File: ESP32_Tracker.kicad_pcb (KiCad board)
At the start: 2 copper layers, 61 parts, among them J1 USB_C_Receptacle_USB2.0_16P, J2 Conn_01x02_Socket, J3 Micro_SD_Card_Det1, SW1 SW_Push, SW2 SW_Push, SW3 SW_Push, U1 XC6220B331MR-G, U2 USBLC6-2SC6, U3 MP2667, U4 SAM-M10Q, U5 LIS2MDL, U6 ESP32-S3-MINI-1

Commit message: initial board layout completed
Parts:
- added C19: 10u, Capacitor_SMD:C_0805_2012Metric, F.Cu at (134.3, 97.2)
- added C20: 0.1u, Capacitor_SMD:C_0805_2012Metric, F.Cu at (132.1, 97.2)
- added C21: 0.1u, Capacitor_SMD:C_0805_2012Metric, B.Cu at (143.8, 105.2)
- added C22: 10u, Capacitor_SMD:C_0805_2012Metric, B.Cu at (141.6, 105.2)
- added J4: MSD-4-A, MSD-4-A_DL:CUI_MSD-4-A, B.Cu at (154.8, 105.5)
- added R19: 10k, Resistor_SMD:R_0805_2012Metric, B.Cu at (142.6, 108.7)
- added R20: 10k, Resistor_SMD:R_0805_2012Metric, B.Cu at (143.7, 99.7)
- added R21: 10k, Resistor_SMD:R_0805_2012Metric, F.Cu at (132.8, 106.0)
- added R22: 10k, Resistor_SMD:R_0805_2012Metric, B.Cu at (142.6, 111.0)
- added R23: 10k, Resistor_SMD:R_0805_2012Metric, B.Cu at (143.7, 97.7)
- added SW4: SW_Push, Button_Switch_SMD:SW_SPST_TS-1088-xR020, F.Cu at (152.6, 103.2)
- added SW5: SW_Push, Button_Switch_SMD:SW_SPST_TL3305C, F.Cu at (158.1, 93.0)
- C1, C5: value 10u -> 1u
- C10: value 0.1u -> 2.2u
- C11, C13: value 0.1u -> 10u
- C12: value 22u -> 10u
- C15, C4: value 10u -> 0.1u
- C16: value 1u -> 0.22u
- C17: value 0.22u -> 2.2u
- C2: value 1u -> 0.1u
- C3: value 2.2u -> 22u
- C7: value 2.2u -> 0.1u
- J3: value Micro_SD_Card_Det1 -> Conn_01x07_Socket; footprint MSD-4-A_DL:CUI_MSD-4-A -> Connector_JST:JST_XH_S7B-XH-A_1x07_P2.50mm_Horizontal
- R1, R3: value 5.1k -> 10k
- R13: value 10k -> 100k
- R16, R2: value 10k -> 2.2k
- R18, TP1, TP2, TP3, TP4, TP5, TP6, TP7, TP8: moved to B.Cu
- R5: value 100k -> 5.1k
- R6: value 2.2k -> 5.1k
- R7: value 2.2k -> 10k
- U1: value XC6220B331MR-G -> USBLC6-2SC6; footprint Package_TO_SOT_SMD:SOT-23-5 -> Package_TO_SOT_SMD:SOT-23-6
- U2: value USBLC6-2SC6 -> ESP32-S3-MINI-1; footprint Package_TO_SOT_SMD:SOT-23-6 -> RF_Module:ESP32-S2-MINI-1
- U4: value SAM-M10Q -> XC6220B331MR-G; footprint RF_GPS:ublox_SAM-M8Q -> Package_TO_SOT_SMD:SOT-23-5
- U6: value ESP32-S3-MINI-1 -> SAM-M10Q; footprint RF_Module:ESP32-S2-MINI-1 -> RF_GPS:ublox_SAM-M8Q
- moved TP8 81.7 mm to (125.6, 68.2)
- moved SW1 76.1 mm to (121.1, 117.5)
- moved TP5 73.6 mm to (124.3, 74.0)
- moved H3 72.4 mm to (121.3, 132.2)
- moved TP2 66.5 mm to (122.3, 82.5)
- moved TP3 65.0 mm to (122.3, 85.7)
- moved TP4 59.5 mm to (128.8, 89.7)
- moved TP1 58.7 mm to (152.3, 68.0)
- moved SW3 57.0 mm to (124.3, 74.0), turned to 90 degrees
- moved J1 57.0 mm to (121.8, 85.0), turned to -90 degrees
- moved U1 56.3 mm to (130.3, 85.0)
- moved R6 55.1 mm to (123.6, 78.5)
- moved H2 54.2 mm to (121.1, 68.2)
- moved U2 53.7 mm to (140.3, 70.7)
- moved U5 52.8 mm to (155.1, 76.0)
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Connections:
- C1 pad 1: +3.3V -> Net-(U2-EN)
- C10 pad 1: +3.3V -> Net-(U3-SYS)
- C11 pad 1: +3.3V -> GND
- C11 pad 2: GND -> Net-(U3-SYS)
- C16 pad 1: Net-(U6-EN) -> Net-(U5-C1)
- C17 pad 1: Net-(U5-C1) -> +3.3V
- C18 pad 1: Net-(U6-IO21) -> +3.3V
- C2 pad 1: GND -> Net-(U2-IO18)
- C2 pad 2: VBUS -> GND
- C3 pad 1: Net-(U1-CE) -> +3.3V
- C4 pad 1: GND -> +3.3V
- C4 pad 2: Net-(U1-CE) -> GND
- C5 pad 2: Net-(J2-Pin_2) -> VBUS
- C6 pad 1: Net-(U3-VDD) -> Net-(U2-IO42)
- C7 pad 1: +3.3V -> Net-(U2-IO21)
- C8 pad 1: +3.3V -> Net-(U3-VDD)
- C9 pad 1: +3.3V -> GND
- C9 pad 2: GND -> Net-(J2-Pin_2)
- J3 pad 1: unconnected-(J3-DAT2-Pad1) -> GND
- J3 pad 2: /SD_CS -> +3.3V
- J3 pad 3: /SD_MOSI -> /MCU/PWR/OLED/SD_SCK
- J3 pad 4: +3.3V -> /MCU/PWR/OLED/SD_MOSI
- J3 pad 5: /SD_CLK -> /MCU/PWR/OLED_CS
- J3 pad 6: GND -> /MCU/PWR/OLED_DC
- J3 pad 7: /SD_MISO -> /MCU/PWR/OLED_RST
- R1 pad 1: GND -> Net-(U2-EN)
- R1 pad 2: Net-(J1-CC1) -> +3.3V
- R10 pad 1: /MAG_DATA -> Net-(U3-NTC)
- R10 pad 2: +3.3V -> VBUS
- R11 pad 1: /MAG_CLK -> Net-(U2-IO42)
- R12 pad 1: /SD_CS -> Net-(U2-IO21)
- R13 pad 1: /SD_MOSI -> +3.3V
- R13 pad 2: +3.3V -> /MCU/PWR/INT
- R14 pad 1: /SD_CLK -> /MCU/PWR/GPS/MAG_DATA
- R15 pad 1: /SD_MISO -> /MCU/PWR/GPS/MAG_CLK
- R16 pad 1: /SD_DETECT -> /MCU/PWR/GPS/MAG_CLK
- R17 pad 1: Net-(D1-A) -> /MCU/PWR/GPS/MAG_DATA
- R17 pad 2: Net-(U6-IO42) -> +3.3V
- R18 pad 1: Net-(U6-IO21) -> +3.3V
- R18 pad 2: +3.3V -> /MCU/PWR/OLED/SD_SCK
- R2 pad 1: Net-(U3-NTC) -> Net-(U2-IO8)
- R2 pad 2: VBUS -> Net-(D1-A)
- R3 pad 1: Net-(J1-CC2) -> Net-(U2-IO18)
- R3 pad 2: GND -> +3.3V
- R4 pad 1: Net-(U3-NTC) -> Net-(U2-IO0)
- R4 pad 2: GND -> +3.3V
- R5 pad 1: +3.3V -> GND
- R5 pad 2: /INT -> Net-(J1-CC1)
- R6 pad 1: /GPS_CLK -> Net-(J1-CC2)
- R6 pad 2: +3.3V -> GND
- R7 pad 1: /GPS_DATA -> /MCU/PWR/BATT_CLK
- R8 pad 1: Net-(U6-EN) -> +3.3V
- R8 pad 2: +3.3V -> /MCU/PWR/BATT_DATA
- R9 pad 1: Net-(U6-IO0) -> Net-(U3-NTC)
- R9 pad 2: +3.3V -> GND
- SW1 pad 2: Net-(U6-EN) -> Net-(U2-EN)
- SW2 pad 1: Net-(U6-IO0) -> Net-(U2-IO18)
- SW3 pad 1: Net-(U6-IO21) -> Net-(U2-IO0)
- TP1 pad 1: VBUS -> Net-(U2-EN)
- TP2 pad 1: +3.3V -> Net-(J1-D--PadA7)
- TP3 pad 1: Net-(U6-EN) -> Net-(J1-D+-PadA6)
- TP4 pad 1: Net-(U6-IO0) -> VBUS
- TP5 pad 1: Net-(J1-D--PadA7) -> Net-(U2-IO0)
- TP6 pad 1: Net-(J1-D+-PadA6) -> Net-(J2-Pin_2)
- TP7 pad 1: Net-(J2-Pin_2) -> Net-(U3-SYS)
- TP8 pad 1: Net-(U1-CE) -> +3.3V
- U1 pad 1: Net-(U1-CE) -> Net-(J1-D--PadA7)
- U1 pad 3: Net-(U1-CE) -> Net-(J1-D+-PadA6)
- U1 pad 4: unconnected-(U1-NC-Pad4) -> /MCU/PWR/USB_P
- U1 pad 5: +3.3V -> VBUS
- U2 pad 1: Net-(J1-D--PadA7) -> GND
- U2 pad 3: Net-(J1-D+-PadA6) -> +3.3V
- U2 pad 4: /USB_P -> Net-(U2-IO0)
- U2 pad 5: VBUS -> unconnected-(U2-IO1-Pad5)
- U2 pad 6: /USB_N -> unconnected-(U2-IO2-Pad6)
- U3 pad 10: Net-(U1-CE) -> Net-(U3-SYS)
- U3 pad 3: /INT -> /MCU/PWR/INT
- U3 pad 6: /BATT_CLK -> /MCU/PWR/BATT_CLK
- U3 pad 7: /BATT_DATA -> /MCU/PWR/BATT_DATA
- U4 pad 1: GND -> Net-(U3-SYS)
- U4 pad 2: +3.3V -> GND
- U4 pad 3: +3.3V -> Net-(U3-SYS)
- U4 pad 4: GND -> unconnected-(U4-NC-Pad4)
- U4 pad 5: GND -> +3.3V
- U5 pad 1: /MAG_CLK -> /MCU/PWR/GPS/MAG_CLK
- U5 pad 4: /MAG_DATA -> /MCU/PWR/GPS/MAG_DATA
- U5 pad 7: /MAG_INT -> /MCU/PWR/MAG_INT
- U6 pad 10: /GPS_CLK -> GND
- U6 pad 11: unconnected-(U6-IO7-Pad11) -> GND
- U6 pad 12: unconnected-(U6-IO8-Pad12) -> /MCU/PWR/GPS/MAG_CLK
- U6 pad 13: /SD_DETECT -> unconnected-(U6-TXD-Pad13)
- U6 pad 14: /SD_CS -> unconnected-(U6-RXD-Pad14)
- U6 pad 15: /SD_MOSI -> GND
- U6 pad 16: /SD_CLK -> GND
- U6 pad 17: /SD_MISO -> +3.3V
- U6 pad 18: /MAG_DATA -> unconnected-(U6-~{RESET}-Pad18)
- U6 pad 19: /MAG_CLK -> unconnected-(U6-EXTINT-Pad19)
- U6 pad 2: GND -> +3.3V
- U6 pad 20: /MAG_INT -> GND
- U6 pad 4: Net-(U6-IO0) -> GND
- U6 pad 5: unconnected-(U6-IO1-Pad5) -> GND
- U6 pad 6: unconnected-(U6-IO2-Pad6) -> GND
- U6 pad 9: /GPS_DATA -> /MCU/PWR/GPS/MAG_DATA
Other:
- board outline added: 45.5 x 75.5 mm
- copper layers 2 -> 4

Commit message: Layout completed
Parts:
- removed H4: MountingHole_Pad, MountingHole:MountingHole_2.2mm_M2_Pad_Via
- added J5: Conn_01x07_Socket, Connector_JST:JST_PH_S7B-PH-K_1x07_P2.00mm_Horizontal, F.Cu at (167.2, 116.0)
- C17: value 2.2u -> 10u; moved to B.Cu
- C18, R16, R17: moved to B.Cu
- C21, C22, J4, R18, R19, R20, R22, R23: moved to F.Cu
- J3: value Conn_01x07_Socket -> Conn_01x03; footprint Connector_JST:JST_XH_S7B-XH-A_1x07_P2.50mm_Horizontal -> Connector_PinHeader_2.54mm:PinHeader_1x03_P2.54mm_Vertical
- SW2, SW4: footprint Button_Switch_SMD:SW_SPST_TS-1088-xR020 -> Button_Switch_SMD:SW_SPST_TL3305C
- moved H2 81.2 mm to (170.1, 133.0)
- moved D1 63.0 mm to (127.2, 70.8), turned to 90 degrees
- moved SW1 61.8 mm to (170.2, 80.0), turned to 180 degrees
- moved R2 60.2 mm to (129.3, 70.8), turned to 90 degrees
- moved C1 57.0 mm to (165.9, 79.5), turned to 90 degrees
- moved R1 53.0 mm to (163.7, 79.4)
- moved SW3 45.8 mm to (170.2, 75.8), turned to 0 degrees
- moved C14 44.9 mm to (127.8, 104.5)
- moved C13 43.5 mm to (130.1, 108.3)
- moved C15 41.5 mm to (130.1, 104.5)
- moved J2 40.5 mm to (120.8, 68.0), turned to 180 degrees
- moved J3 39.4 mm to (160.5, 74.5), turned to 180 degrees
- moved R4 38.8 mm to (166.2, 74.7)
- moved TP6 38.3 mm to (123.0, 75.5)
- moved C20 36.6 mm to (164.2, 115.0), turned to -90 degrees
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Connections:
- net Net-(J2-Pin_2) renamed +BATT
- C2 pad 1: Net-(U2-IO18) -> /MCU/PWR/SW_TOGGLE
- C6 pad 1: Net-(U2-IO42) -> /MCU/PWR/SW_PWR
- C7 pad 1: Net-(U2-IO21) -> /MCU/PWR/SW_LOG
- J1 pad A6: Net-(J1-D+-PadA6) -> unconnected-(J1-D+-PadA6)
- J1 pad A7: Net-(J1-D--PadA7) -> unconnected-(J1-D--PadA7)
- J1 pad B6: Net-(J1-D+-PadA6) -> unconnected-(J1-D+-PadB6)
- J1 pad B7: Net-(J1-D--PadA7) -> unconnected-(J1-D--PadB7)
- J3 pad 1: GND -> /MCU/PWR/TX
- J3 pad 2: +3.3V -> /MCU/PWR/RX
- J3 pad 3: /MCU/PWR/OLED/SD_SCK -> GND
- R11 pad 1: Net-(U2-IO42) -> /MCU/PWR/SW_PWR
- R12 pad 1: Net-(U2-IO21) -> /MCU/PWR/SW_LOG
- R13 pad 2: /MCU/PWR/INT -> /MCU/PWR/BATT_INT
- R2 pad 1: Net-(U2-IO8) -> Net-(U2-IO2)
- R3 pad 1: Net-(U2-IO18) -> /MCU/PWR/SW_TOGGLE
- SW2 pad 1: Net-(U2-IO18) -> GND
- SW2 pad 2: GND -> /MCU/PWR/SW_TOGGLE
- SW4 pad 1: Net-(U2-IO42) -> /MCU/PWR/SW_PWR
- SW5 pad 1: Net-(U2-IO21) -> /MCU/PWR/SW_LOG
- TP2 pad 1: Net-(J1-D--PadA7) -> /MCU/PWR/TX
- TP3 pad 1: Net-(J1-D+-PadA6) -> /MCU/PWR/RX
- U1 pad 1: Net-(J1-D--PadA7) -> unconnected-(U1-I/O1-Pad1)
- U1 pad 3: Net-(J1-D+-PadA6) -> unconnected-(U1-I/O2-Pad3)
- U1 pad 4: /MCU/PWR/USB_P -> unconnected-(U1-I/O2-Pad4)
- U1 pad 6: /MCU/PWR/USB_N -> unconnected-(U1-I/O1-Pad6)
- U2 pad 10: /MCU/PWR/GPS/MAG_CLK -> /MCU/PWR/BATT_INT
- U2 pad 11: /MCU/PWR/OLED_CS -> unconnected-(U2-IO7-Pad11)
- U2 pad 12: Net-(U2-IO8) -> unconnected-(U2-IO8-Pad12)
- U2 pad 13: /MCU/PWR/SD_DETECT -> unconnected-(U2-IO9-Pad13)
- U2 pad 14: /MCU/PWR/SD_CS -> unconnected-(U2-IO10-Pad14)
- U2 pad 15: /MCU/PWR/OLED/SD_MOSI -> unconnected-(U2-IO11-Pad15)
- U2 pad 16: /MCU/PWR/OLED/SD_SCK -> /MCU/PWR/MAG_INT
- U2 pad 17: /MCU/PWR/SD_MISO -> /MCU/PWR/GPS/MAG_DATA
- U2 pad 18: unconnected-(U2-IO14-Pad18) -> /MCU/PWR/GPS/MAG_CLK
- U2 pad 19: unconnected-(U2-IO15-Pad19) -> /MCU/PWR/SD_DETECT
- U2 pad 20: /MCU/PWR/MAG_INT -> /MCU/PWR/SD_MISO
- U2 pad 21: unconnected-(U2-IO17-Pad21) -> /MCU/PWR/OLED/SD_SCK
- U2 pad 22: Net-(U2-IO18) -> /MCU/PWR/OLED/SD_MOSI
- U2 pad 23: /MCU/PWR/USB_N -> unconnected-(U2-USB_D--Pad23)
- U2 pad 24: /MCU/PWR/USB_P -> unconnected-(U2-USB_D+-Pad24)
- U2 pad 25: Net-(U2-IO21) -> /MCU/PWR/SD_CS
- U2 pad 26: /MCU/PWR/OLED_RST -> /MCU/PWR/OLED_CS
- U2 pad 28: unconnected-(U2-IO33-Pad28) -> /MCU/PWR/OLED_DC
- U2 pad 29: /MCU/PWR/BATT_DATA -> /MCU/PWR/OLED_RST
- U2 pad 31: /MCU/PWR/BATT_CLK -> unconnected-(U2-IO35-Pad31)
- U2 pad 33: unconnected-(U2-IO37-Pad33) -> /MCU/PWR/SW_LOG
- U2 pad 34: unconnected-(U2-IO38-Pad34) -> /MCU/PWR/SW_PWR
- U2 pad 35: unconnected-(U2-IO39-Pad35) -> /MCU/PWR/SW_TOGGLE
- U2 pad 38: Net-(U2-IO42) -> unconnected-(U2-IO42-Pad38)
- U2 pad 39: unconnected-(U2-TXD0-Pad39) -> /MCU/PWR/TX
- U2 pad 40: unconnected-(U2-RXD0-Pad40) -> /MCU/PWR/RX
- U2 pad 6: unconnected-(U2-IO2-Pad6) -> Net-(U2-IO2)
- U2 pad 8: /MCU/PWR/OLED_DC -> /MCU/PWR/BATT_DATA
- U2 pad 9: /MCU/PWR/GPS/MAG_DATA -> /MCU/PWR/BATT_CLK
- U3 pad 3: /MCU/PWR/INT -> /MCU/PWR/BATT_INT
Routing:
- net GND: track 0.00 -> 95.8 mm, vias 0 -> 183
- net +3.3V: track 0.00 -> 71.5 mm, vias 0 -> 29
- net /MCU/PWR/OLED/SD_SCK: track 0.00 -> 56.2 mm, vias 0 -> 2
- net /MCU/PWR/GPS/MAG_DATA: track 0.00 -> 54.7 mm, vias 0 -> 2
- net /MCU/PWR/OLED/SD_MOSI: track 0.00 -> 52.7 mm, vias 0 -> 2
- net /MCU/PWR/GPS/MAG_CLK: track 0.00 -> 50.0 mm, vias 0 -> 2
- net /MCU/PWR/SD_CS: track 0.00 -> 40.5 mm
- net /MCU/PWR/OLED_CS: track 0.00 -> 35.8 mm
- net /MCU/PWR/SD_MISO: track 0.00 -> 34.9 mm
- net /MCU/PWR/SD_DETECT: track 0.00 -> 34.6 mm
- net Net-(U2-IO0): track 0.00 -> 34.2 mm, vias 0 -> 2
- net /MCU/PWR/SW_LOG: track 0.00 -> 32.9 mm
- net /MCU/PWR/OLED_DC: track 0.00 -> 32.4 mm
- net /MCU/PWR/OLED_RST: track 0.00 -> 30.5 mm
- net /MCU/PWR/MAG_INT: track 0.00 -> 27.3 mm
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- added copper zone on F.Cu, net +3.3V
- added copper zone on In2.Cu, net +3.3V
- added copper zone on F.Cu, net +BATT
- added copper zone on B.Cu, net GND
- added copper zone on F.Cu, net GND
- added copper zone on In1.Cu, net GND
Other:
- board size 45.5 x 75.5 mm -> 60 x 75 mm
- board text added: "Matthew Tubbin REV 1.0 1/13/2026 ECE212"

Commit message: modified layout
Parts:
- added TP9: TestPoint, TestPoint:TestPoint_Pad_D1.5mm, B.Cu at (147.7, 88.5)
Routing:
- net +3.3V: track 71.5 -> 64.4 mm, vias 29 -> 34
- net GND: track 95.8 -> 99.2 mm, vias 183 -> 186
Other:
- board text added: "3.3V"
- board text added: "BATT"
- board text added: "BOOT"
- board text added: "GND"
- board text added: "LOG"
- board text added: "PWR"
- board text added: "RESET"
- board text added: "RX"
- board text added: "SYS"
- board text added: "TOGGLE"
- board text added: "TX"
- board text added: "VBUS"

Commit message: modified and labeled layout
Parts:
- added C23: 0.1u, Capacitor_SMD:C_0805_2012Metric, B.Cu at (116.8, 120.5)
- moved C17 5.74 mm to (127.3, 135.0), turned to 0 degrees
- moved C13 4.78 mm to (132.7, 104.3)
- moved C15 4.78 mm to (132.7, 100.5)
- moved C16 4.78 mm to (135.2, 96.8)
- moved R14 4.78 mm to (138.2, 95.5)
- moved U5 4.78 mm to (135.9, 100.2)
- moved C14 4.78 mm to (130.4, 100.5)
- moved R15 4.78 mm to (139.2, 100.2)
- moved TP5 3.76 mm to (144.2, 74.5)
- moved TP1 3.50 mm to (157.0, 72.8)
- moved C18 2.87 mm to (127.3, 132.8)
- moved R16 2.47 mm to (127.3, 113.7)
- moved U6 2.47 mm to (126.3, 123.5)
- moved R17 2.47 mm to (136.2, 122.4)
- moved R23 0.29 mm to (142.8, 112.8)
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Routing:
- net GND: track 99.2 -> 123.0 mm, vias 186 -> 218
- net /MCU/PWR/MAG_INT: track 27.3 -> 22.2 mm
- net +3.3V: track 64.4 -> 59.6 mm, vias 34 -> 33
- net Net-(U2-IO0): track 34.2 -> 31.3 mm
- net Net-(U2-EN): track 24.5 -> 22.1 mm
- net /MCU/PWR/GPS/MAG_CLK: track 50.0 -> 47.6 mm
- net /MCU/PWR/GPS/MAG_DATA: track 54.7 -> 52.3 mm
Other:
- board text added: "Matthew Tubbin REV 1.0 1/14/2026 ECE-212"
- board text removed: "Matthew Tubbin REV 1.0 1/13/2026 ECE212"

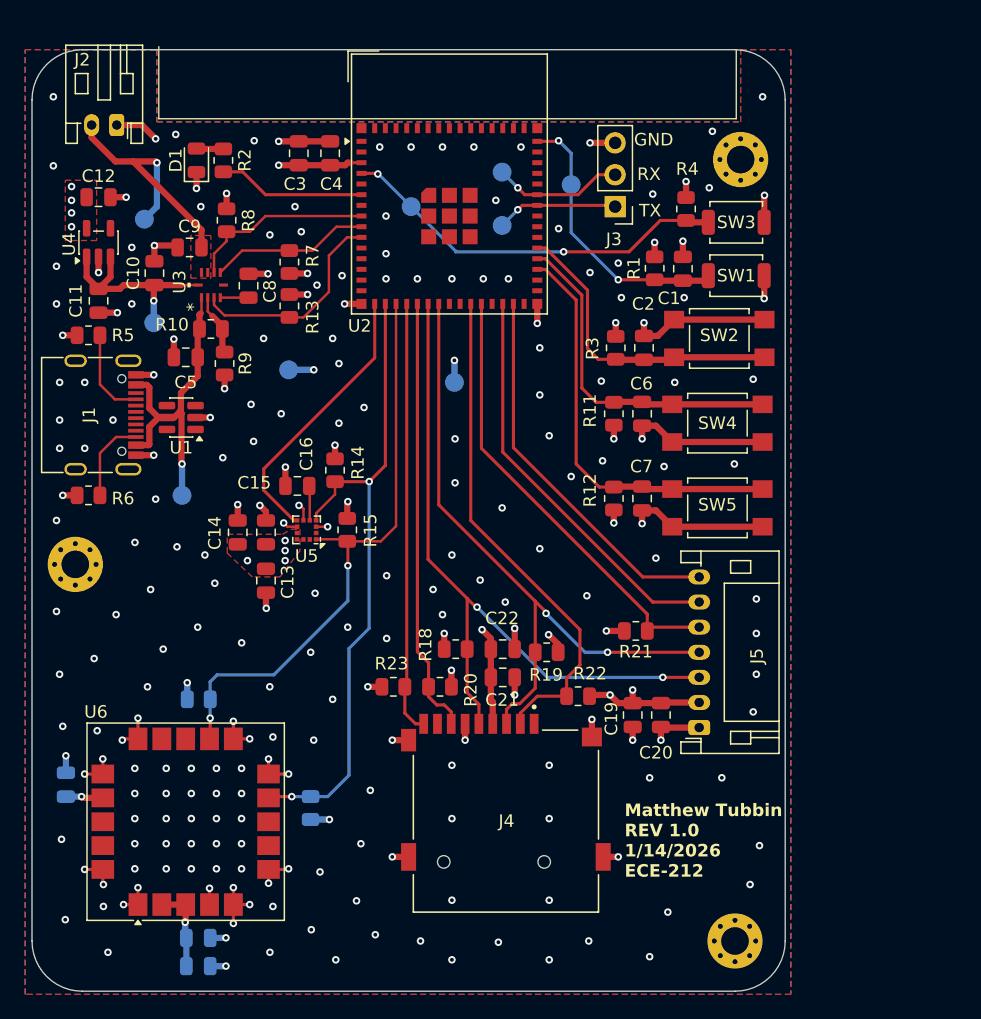
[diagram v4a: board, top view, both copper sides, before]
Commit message: added USBC programming
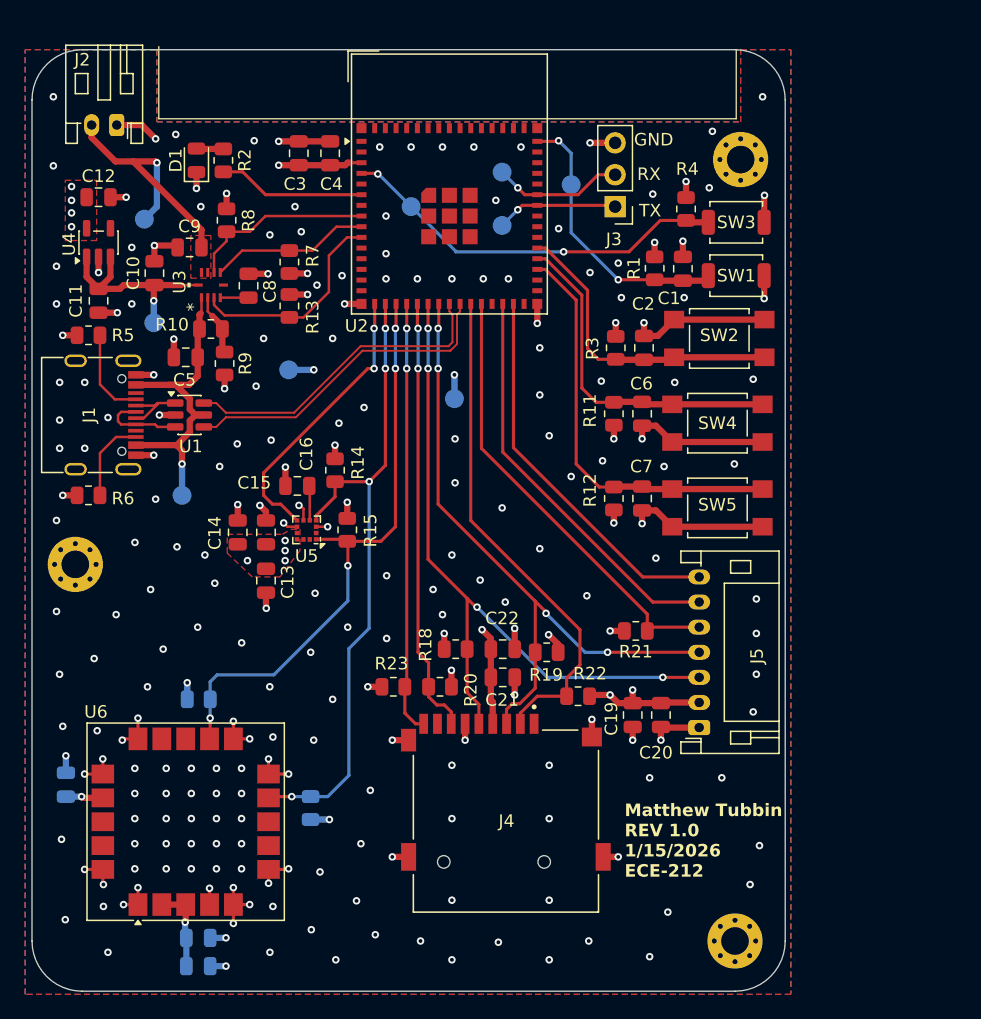
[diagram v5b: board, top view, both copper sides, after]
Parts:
- moved TP9 1.30 mm to (147.7, 89.8)
- moved U1 0.69 mm to (126.6, 91.1), turned to 0 degrees
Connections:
- J1 pad A6: unconnected-(J1-D+-PadA6) -> Net-(J1-D+-PadA6)
- J1 pad A7: unconnected-(J1-D--PadA7) -> Net-(J1-D--PadA7)
- J1 pad B6: unconnected-(J1-D+-PadB6) -> Net-(J1-D+-PadA6)
- J1 pad B7: unconnected-(J1-D--PadB7) -> Net-(J1-D--PadA7)
- U1 pad 1: unconnected-(U1-I/O1-Pad1) -> Net-(J1-D--PadA7)
- U1 pad 3: unconnected-(U1-I/O2-Pad3) -> Net-(J1-D+-PadA6)
- U1 pad 4: unconnected-(U1-I/O2-Pad4) -> /MCU/PWR/USB_D+
- U1 pad 6: unconnected-(U1-I/O1-Pad6) -> /MCU/PWR/USB_D-
- U2 pad 23: unconnected-(U2-USB_D--Pad23) -> /MCU/PWR/USB_D-
- U2 pad 24: unconnected-(U2-USB_D+-Pad24) -> /MCU/PWR/USB_D+
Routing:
- net /MCU/PWR/USB_D+: track 0.00 -> 26.2 mm
- net /MCU/PWR/USB_D-: track 0.00 -> 25.6 mm
- net Net-(J1-D+-PadA6): track 0.00 -> 6.77 mm
- net Net-(J1-D--PadA7): track 0.00 -> 5.50 mm
- net VBUS: track 25.8 -> 26.4 mm
- net /MCU/PWR/MAG_INT: track 22.2 -> 22.7 mm, vias 0 -> 2
- net GND: track 123.0 -> 123.2 mm, vias 218 -> 217
- net /MCU/PWR/OLED/SD_MOSI: track 52.7 -> 52.9 mm, vias 2 -> 4
- net /MCU/PWR/GPS/MAG_CLK: track 47.6 -> 47.7 mm, vias 2 -> 4
- net /MCU/PWR/SD_MISO: vias 0 -> 2
- net /MCU/PWR/SD_DETECT: vias 0 -> 2
- net /MCU/PWR/OLED/SD_SCK: vias 2 -> 4
- net /MCU/PWR/GPS/MAG_DATA: vias 2 -> 4
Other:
- board text added: "Matthew Tubbin REV 1.0 1/15/2026 ECE-212"
- board text removed: "Matthew Tubbin REV 1.0 1/14/2026 ECE-212"
